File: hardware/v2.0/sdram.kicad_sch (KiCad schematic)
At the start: 10 parts, among them IC1 IS42S16160J-6BLI, U1 ECP5-CABGA256

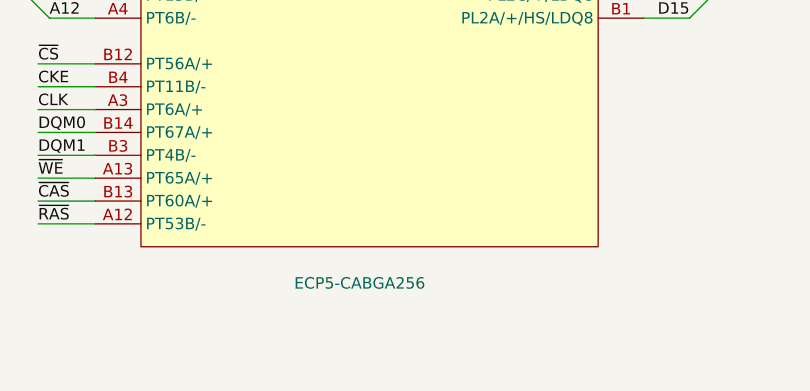
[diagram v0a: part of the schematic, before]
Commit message: Initial plan for adding an external ADC
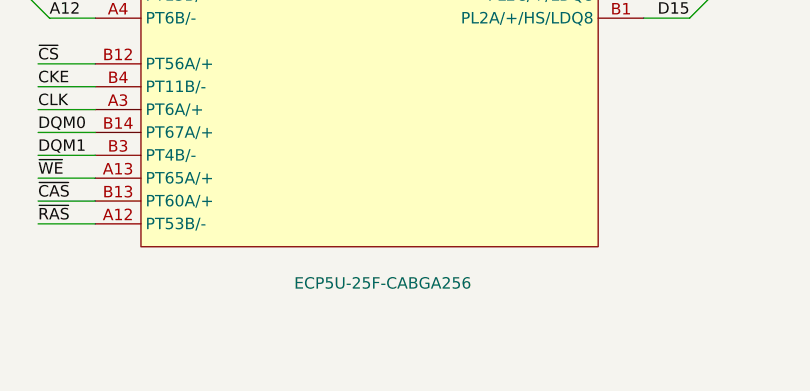
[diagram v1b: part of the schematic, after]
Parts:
- U1: value ECP5-CABGA256 -> ECP5U-25F-CABGA256; LCSC Link https://lcsc.com/product-detail/Programmable-Logic-Device-C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 -> (none); LCSC Part # C1521614 -> (none); Manufactuer Part Number LFE5U-25F-6BG256C -> (none)
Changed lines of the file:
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@@
 			)
 		)
-		(property "Value" "ECP5-CABGA256"
+		(property "Value" "ECP5U-25F-CABGA256"
 			(at 83.058 137.414 0)
 			(effects
@@
 			(effects
 				(font
-					(size 1.27 1.27)
-				)
-				(hide yes)
-			)
-		)
-		(property "LCSC Link" "https://lcsc.com/product-detail/Programmable-Logic-Device-CPLDs-FPGAs_Lattice-LFE5U-25F-6BG256C_C1521614.html"
-			(at 91.44 100.33 0)
-			(effects
-				(font
-					(size 1.27 1.27)
-				)
-				(hide yes)
-			)
-		)
-		(property "Manufactuer Part Number" "LFE5U-25F-6BG256C"
-			(at 91.44 100.33 0)
-			(effects
-				(font
-					(size 1.27 1.27)
-				)
-				(hide yes)
-			)
-		)
-		(property "LCSC Part #" "C1521614"
-			(at 91.44 100.33 0)
-			(effects
-				(font
-					(size 1.27 1.27)
-				)
-				(hide yes)
-			)
-		)
-		(property "Note" ""
-			(at 91.44 100.33 0)
-			(effects
-				(font
-					(size 1.27 1.27)
-				)
-				(hide yes)
-			)
-		)
-		(property "Notes" ""
-			(at 91.44 100.33 0)
-			(effects
-				(font
